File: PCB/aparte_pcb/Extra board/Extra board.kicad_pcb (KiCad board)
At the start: 2 copper layers, 8 parts, among them J1 Conn_01x10_Pin, J2 Conn_01x04_Pin, J3 Conn_01x10_Pin, J4 Conn_01x04_Pin, U2 MCP23017_SP

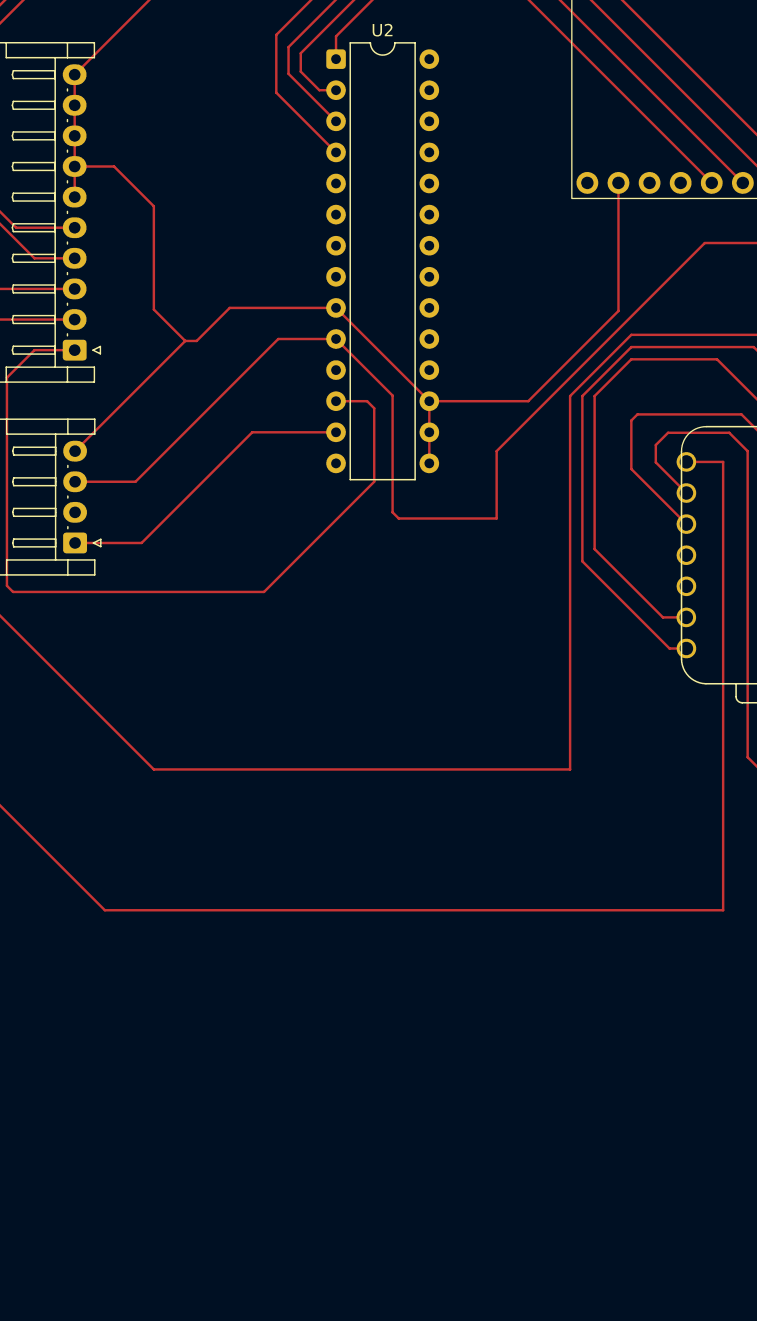
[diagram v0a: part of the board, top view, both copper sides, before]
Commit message: Communication module.
Added Communication module to extra PCB, but the power requerments are either our battery power or 3v, but current lines only allow 5v, so either new lines or an power conversion component.
Need to discuss best option with team.
Also TX/RX lines optional but not available. I2C to UART module?
Also need to discuss.

Signed-off-by: Abel Tim <git@abeltim.com>
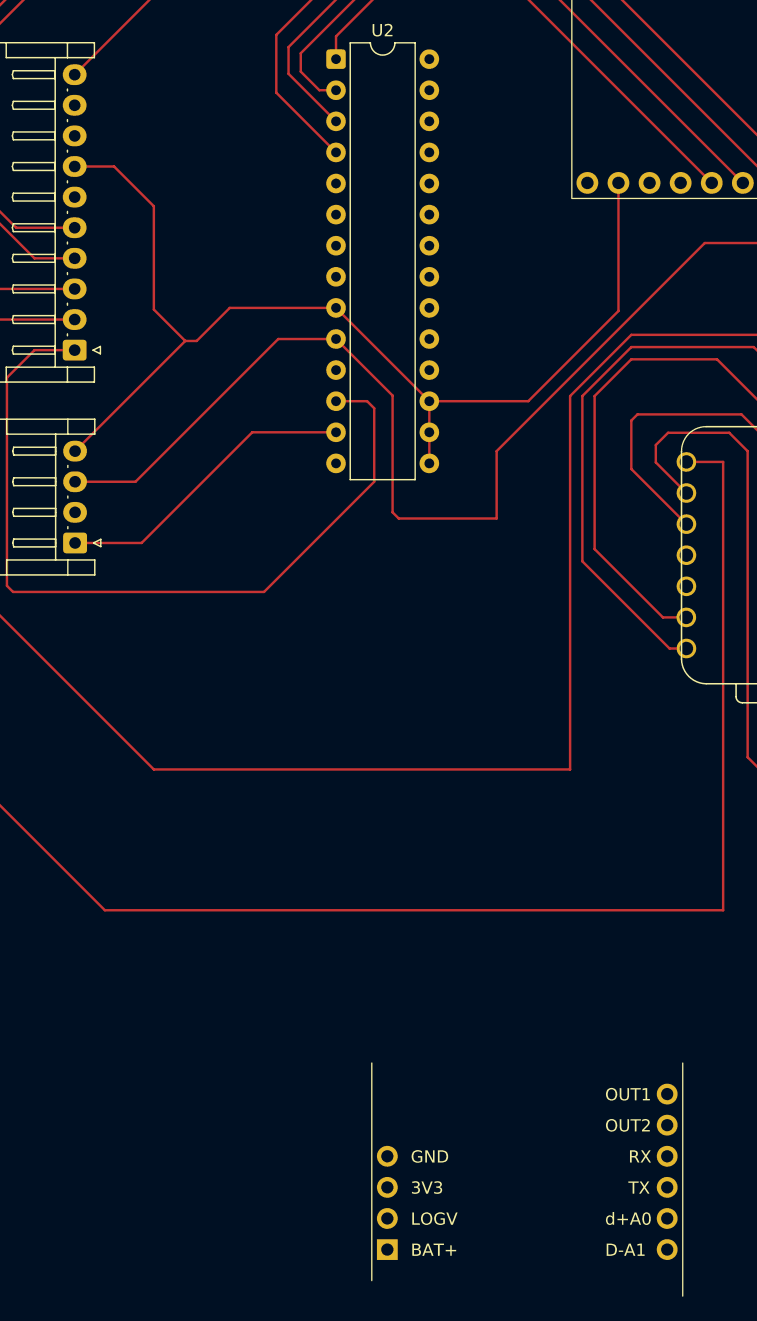
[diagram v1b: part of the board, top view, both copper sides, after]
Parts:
- added U1: ~, Library:soccer-communication-module, F.Cu at (128.7, 139.6)
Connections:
- J1 pad 6: GND -> OUT2
- J1 pad 7: GND -> D+A0
- J1 pad 8: GND -> D-A1
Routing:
- net GND: track 309.2 -> 299.2 mm
